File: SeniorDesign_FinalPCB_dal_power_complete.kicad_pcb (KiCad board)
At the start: 2 copper layers, 172.7 x 167.4 mm, 220 parts, among them J1 5000, J10 5000, J2 5000, J3 5000, J4 5000, J5 5000, J6 5000, J7 5000, J8 5000, J9 5000, Q1 Si7450DP, Q10 Si7450DP, Q11 Si7450DP, Q12 Si7450DP, Q13 Si7450DP, Q14 Si7450DP, Q15 Si7450DP, Q16 Si7450DP, Q2 Si7450DP, Q3 Si7450DP, Q4 Si7450DP, Q5 Si7450DP, Q6 Si7450DP, Q7 Si7450DP, Q8 Si7450DP, Q9 Si7450DP, U1 Transducer, U10 Transducer, U11 Transducer, U12 Transducer, U13 Transducer, U14 Transducer, U15 Transducer, U16 Transducer, U17 Transducer, U18 Transducer, U19 Transducer, U2 Transducer, U20 Transducer, U21 Transducer, U22 Transducer, U23 Transducer, U24 Transducer, U25 Transducer, U26 Transducer, U27 Transducer, U28 Transducer, U29 Transducer, U3 Transducer, U30 Transducer, U31 Transducer, U32 Transducer, U33 Transducer, U34 Transducer, U35 Transducer, U36 Transducer, U37 Transducer, U38 Transducer, U39 Transducer, U4 Transducer, U40 Transducer, U41 Transducer, U42 Transducer, U43 Transducer, U44 Transducer, U45 Transducer, U46 Transducer, U47 Transducer, U48 Transducer, U49 Transducer, U5 Transducer, U50 Transducer, U51 Transducer, U52 Transducer, U53 Transducer, U54 Transducer, U55 Transducer, U56 Transducer, U57 Transducer, U58 Transducer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

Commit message: Update files for pcb
Opened project prior to creation of git so all changes were not tracked.
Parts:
- added J11: POWER, SeniorDesign:Screw Terminal 1x4, F.Cu at (468.9, 66.1)
- added U65: CMOD_A7, SeniorDesign:CMOD A7, F.Cu at (464.8, 121.4)
- moved C5 291.8 mm to (464.3, 82.0), turned to 90 degrees
- moved C6 291.0 mm to (464.3, 66.8), turned to -90 degrees
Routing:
- net VPP: track 75.6 -> 80.2 mm
- net +12V: track 134.8 -> 139.4 mm

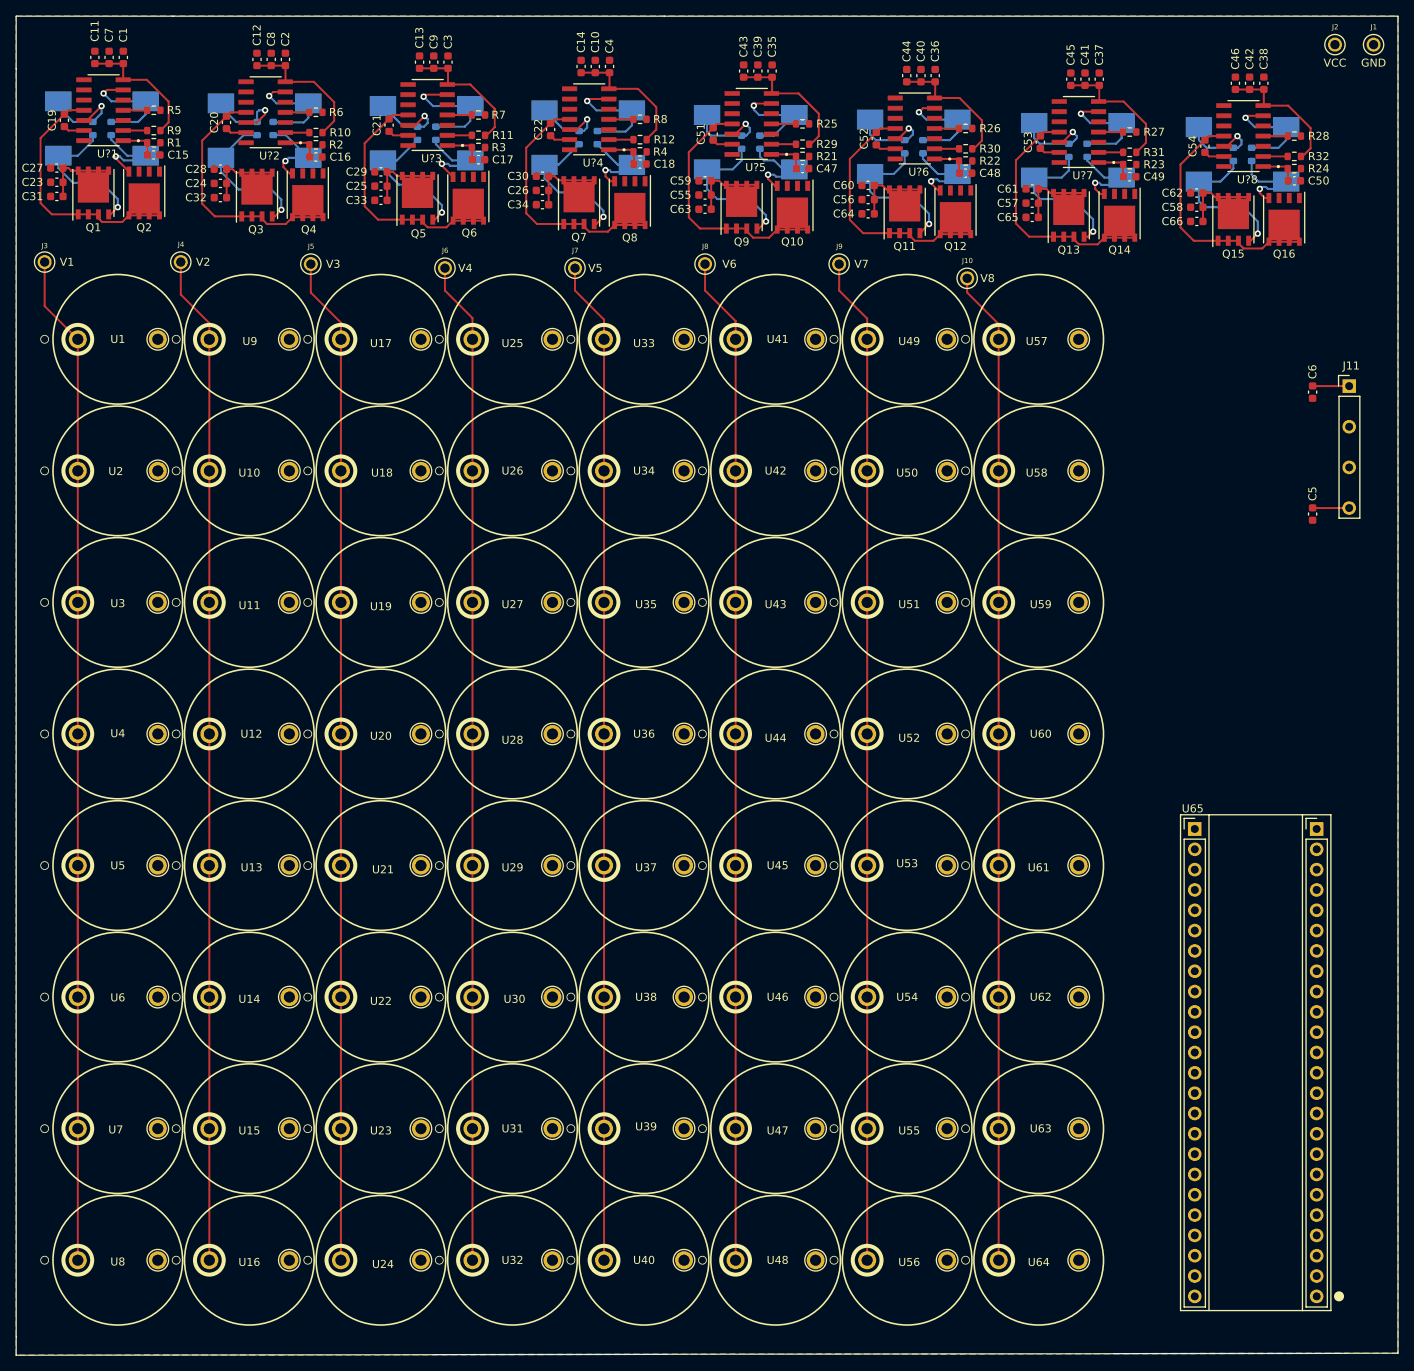
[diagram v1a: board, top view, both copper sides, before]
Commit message: trace widths in amplifier channel adjusted
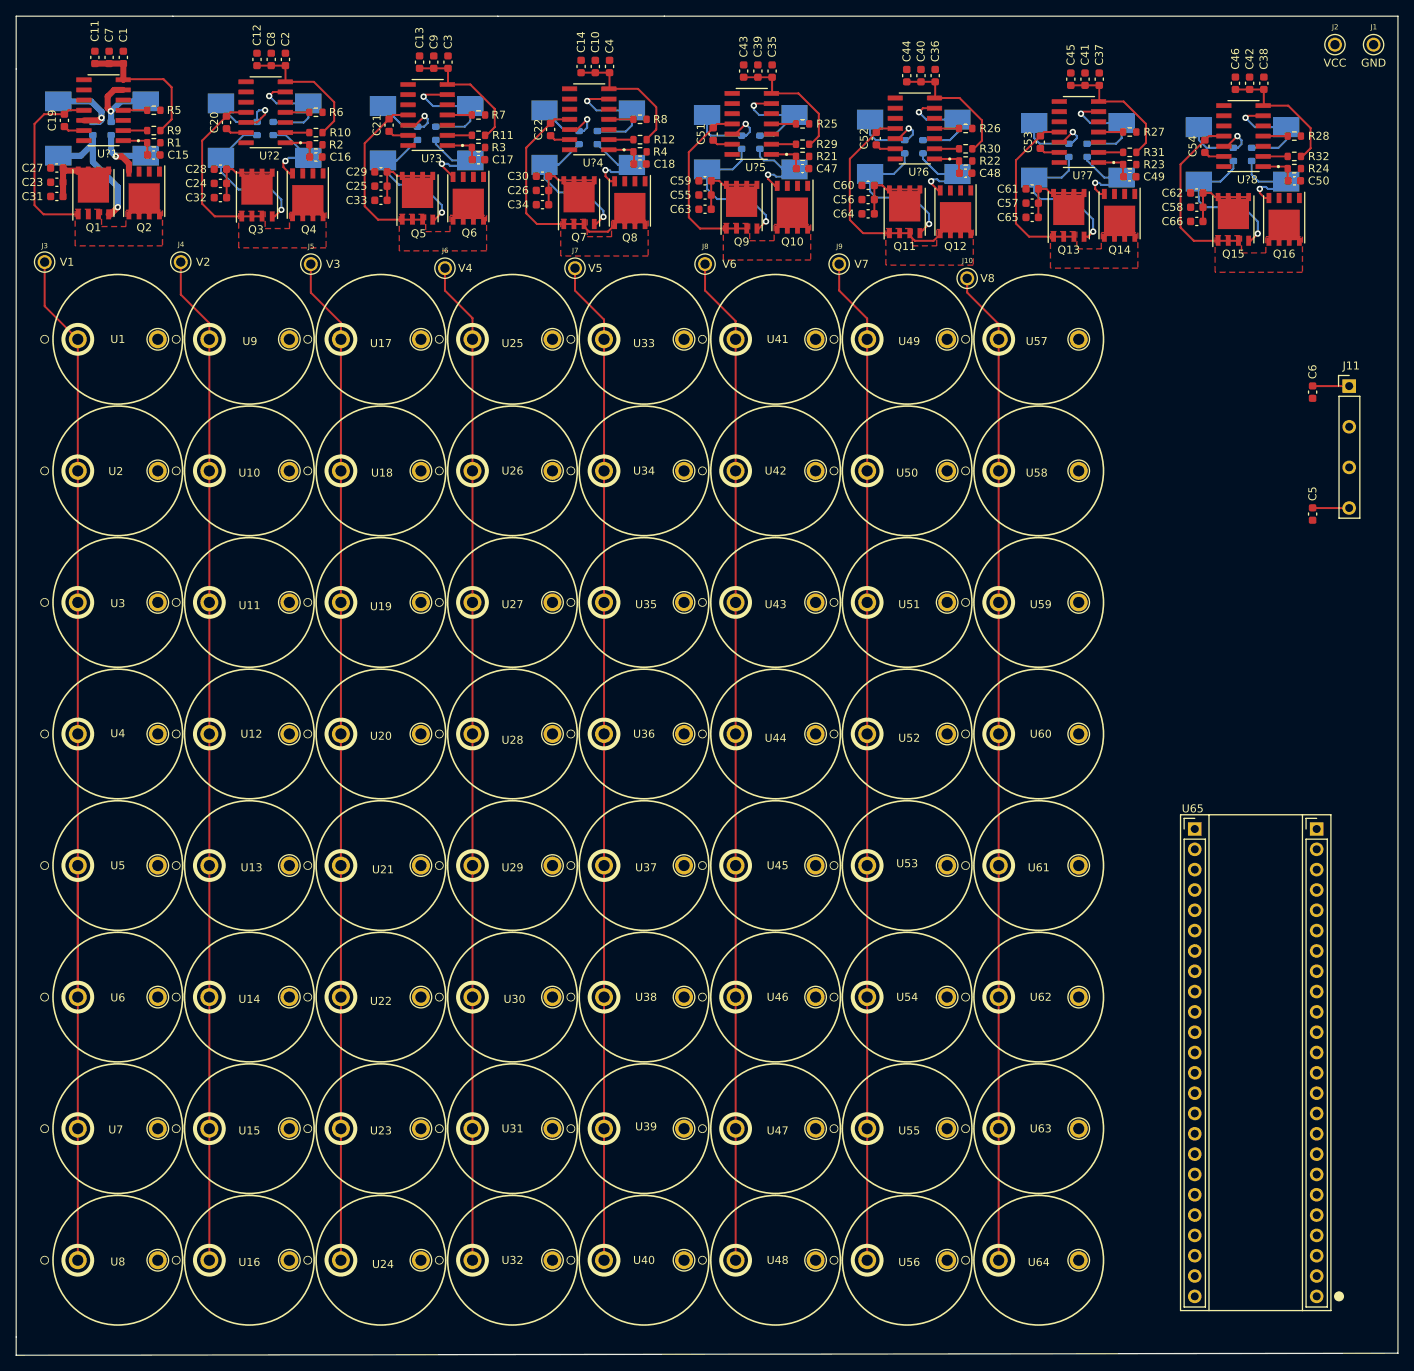
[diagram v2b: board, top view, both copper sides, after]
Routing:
- net /pwm_driver/COL1_OUT: track 31.5 -> 23.0 mm
- net /pwm_driver/COL5_OUT: track 31.6 -> 23.2 mm
- net /pwm_driver/COL2_OUT: track 31.6 -> 23.3 mm
- net /pwm_driver/COL7_OUT: track 31.2 -> 23.0 mm
- net /pwm_driver/COL8_OUT: track 31.2 -> 23.0 mm
- net /pwm_driver/COL3_OUT: track 31.2 -> 23.0 mm
- net Net-(D2-Pad1): track 14.6 -> 10.5 mm
- net /pwm_driver/COL6_OUT: track 31.6 -> 27.8 mm
- net /pwm_driver/COL4_OUT: track 31.4 -> 27.6 mm
- net Net-(D2-Pad2): track 13.7 -> 12.0 mm
- net +12V: track 139.4 -> 141.1 mm
- net Net-(D1-Pad2): track 18.9 -> 17.4 mm
- added copper zone on F.Cu, net /pwm_driver/COL1_OUT
- added copper zone on F.Cu, net /pwm_driver/COL2_OUT
- added copper zone on F.Cu, net /pwm_driver/COL3_OUT
- added copper zone on F.Cu, net /pwm_driver/COL4_OUT
- added copper zone on F.Cu, net /pwm_driver/COL5_OUT
- added copper zone on F.Cu, net /pwm_driver/COL6_OUT
- added copper zone on F.Cu, net /pwm_driver/COL7_OUT
- added copper zone on F.Cu, net /pwm_driver/COL8_OUT
- removed copper zone on B.Cu, net GND
- removed copper zone on F.Cu, net GND

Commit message: Add the memes, temp place on board
m e m e s
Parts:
- added G***: LOGO, SeniorDesign:praise, F.Cu at (461.8, 98.3)
- added G***: LOGO, SeniorDesign:washington, F.Cu at (446.5, 94.7)
- added G***: LOGO, SeniorDesign:resistance, F.Cu at (458.6, 93.6)

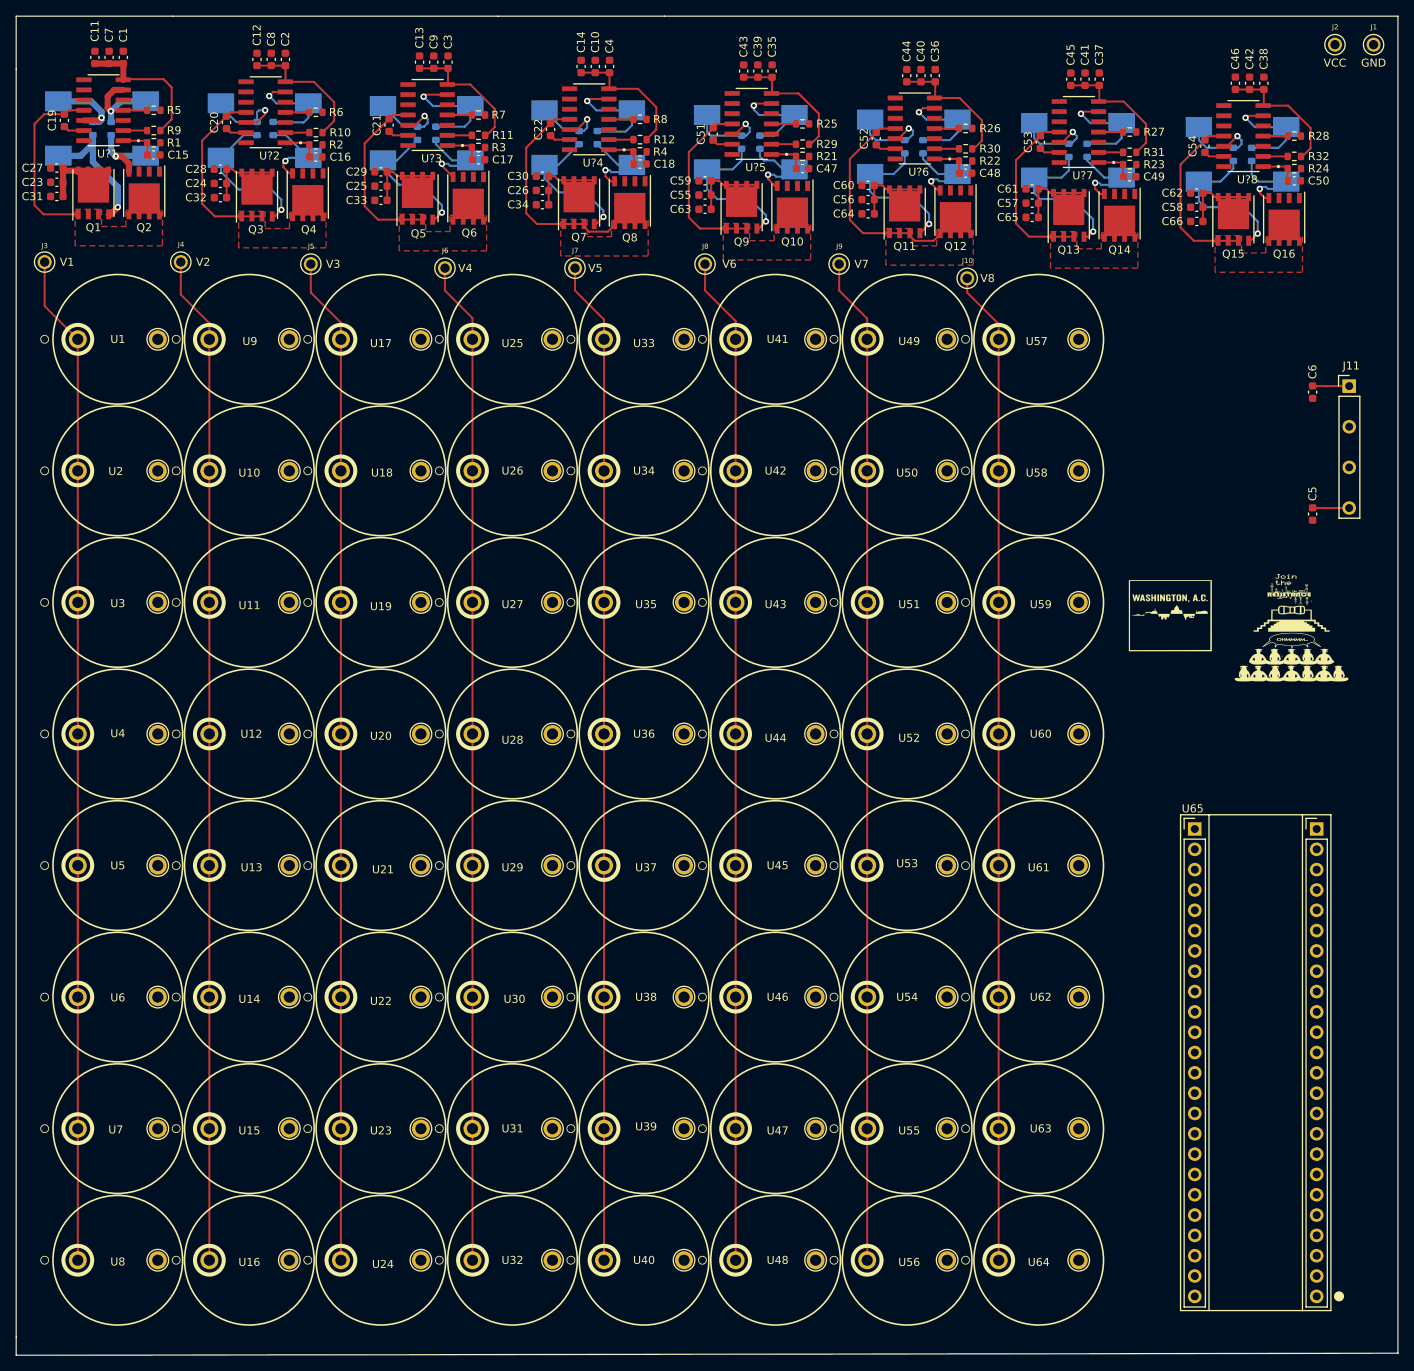
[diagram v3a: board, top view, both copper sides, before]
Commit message: Fixed transducer trace widths and via net names.
Also adds WELAC logo and silkscreen board name + contributors
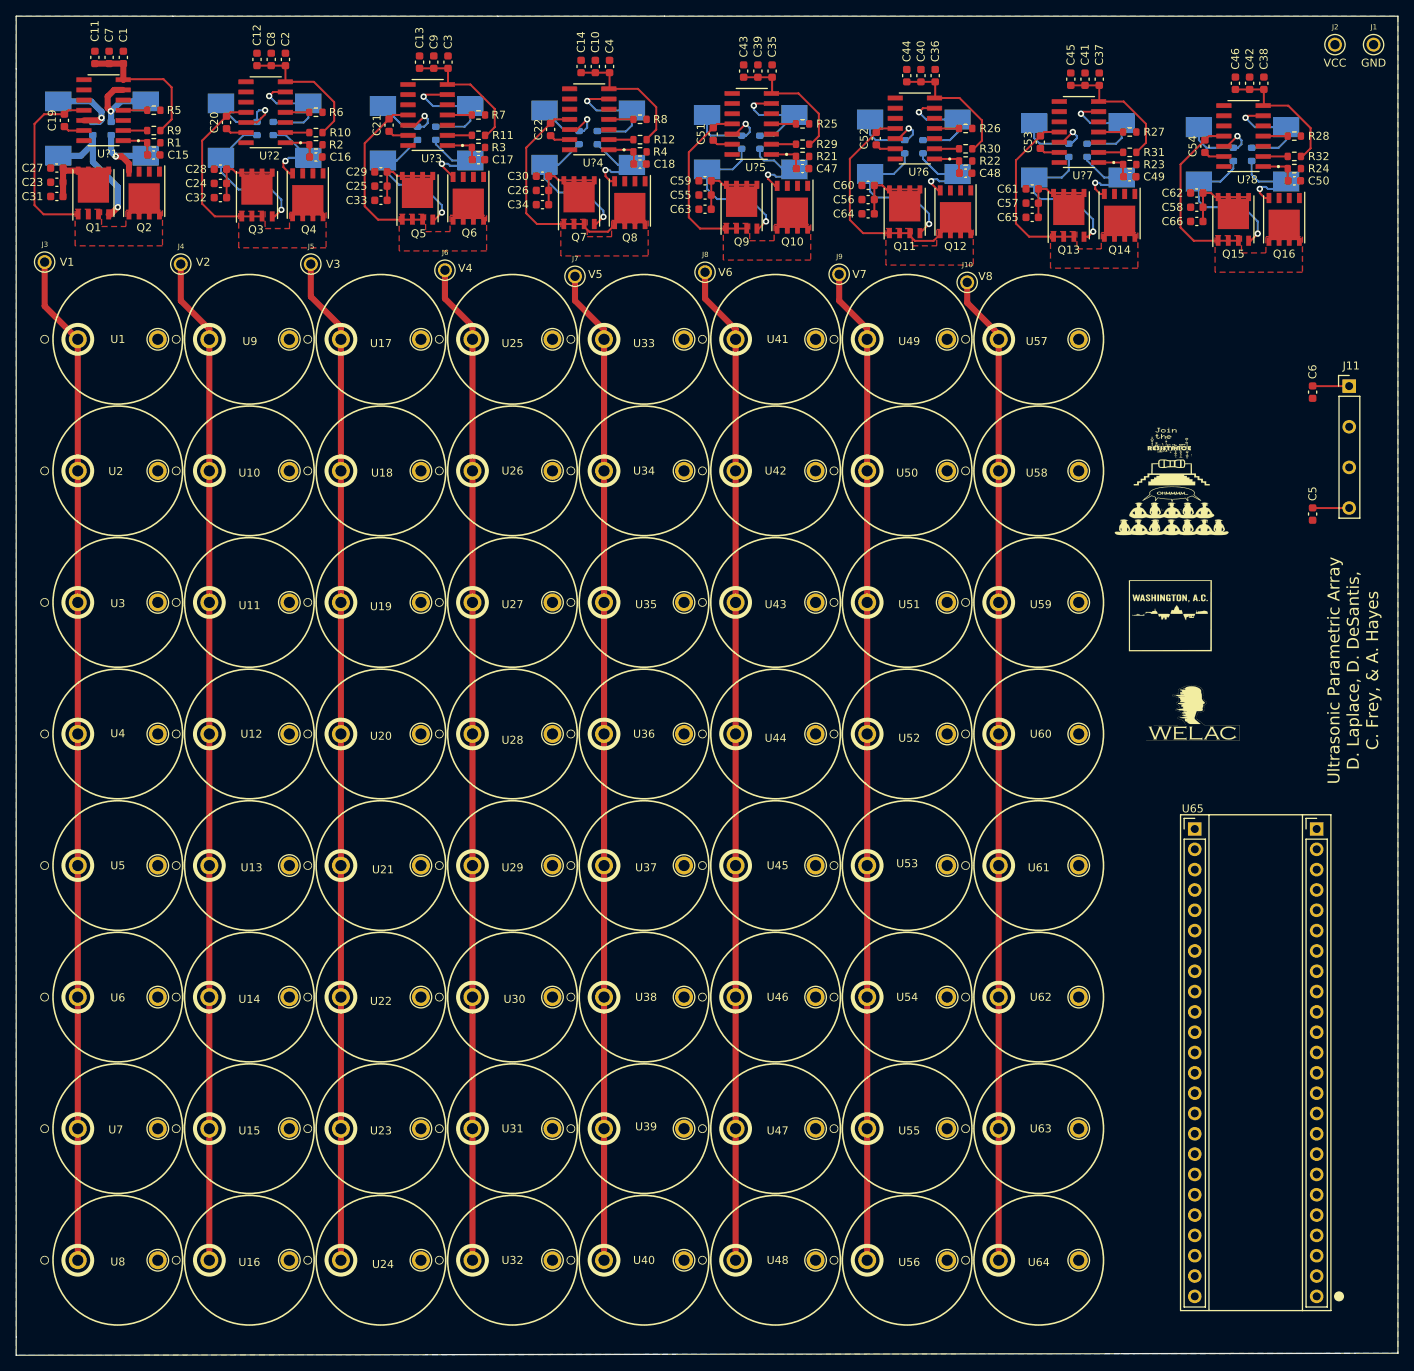
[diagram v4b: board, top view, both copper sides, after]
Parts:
- added G***: LOGO, SeniorDesign:pcblogo, F.Cu at (449.3, 107.2)
- moved G*** 23.6 mm to (443.6, 75.3)
- moved G*** 23.6 mm to (446.8, 80.0)
- moved J9 1.27 mm to (405.1, 52.1)
- moved J8 1.02 mm to (388.4, 51.8)
- moved J7 1.02 mm to (372.1, 52.3)
- moved J10 0.51 mm to (421.1, 53.1)
- moved J4 0.25 mm to (322.8, 50.8)
- moved J6 0.25 mm to (355.9, 51.6)
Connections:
- net V1 renamed COL1_OUT
- net V2 renamed COL2_OUT
- net V3 renamed COL3_OUT
- net V4 renamed COL4_OUT
- net V5 renamed COL5_OUT
- net V6 renamed COL6_OUT
- net V7 renamed COL7_OUT
- net V8 renamed COL8_OUT
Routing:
- net COL1_OUT: track 142.9 -> 126.5 mm
- net COL7_OUT: track 126.0 -> 124.8 mm
- net COL6_OUT: track 126.1 -> 125.1 mm
- net COL5_OUT: track 125.6 -> 124.6 mm
- net COL8_OUT: track 124.5 -> 124.0 mm
- added copper zone on B.Cu, net GND
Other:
- board text added: "Ultrasonic Parametric Array D. Laplace, D. DeSantis, C. Frey, & A. Hayes"
